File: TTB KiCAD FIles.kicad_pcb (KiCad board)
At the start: 2 copper layers, 201.2 x 86.7 mm, 10 parts, among them J1 PJ-102A, J2 Spare_Pwr_Header, J3 Mtr_Driver_Logic, J4 Relay_12V, J5 Relay_GND, J6 Mtr_Driver_Pwr

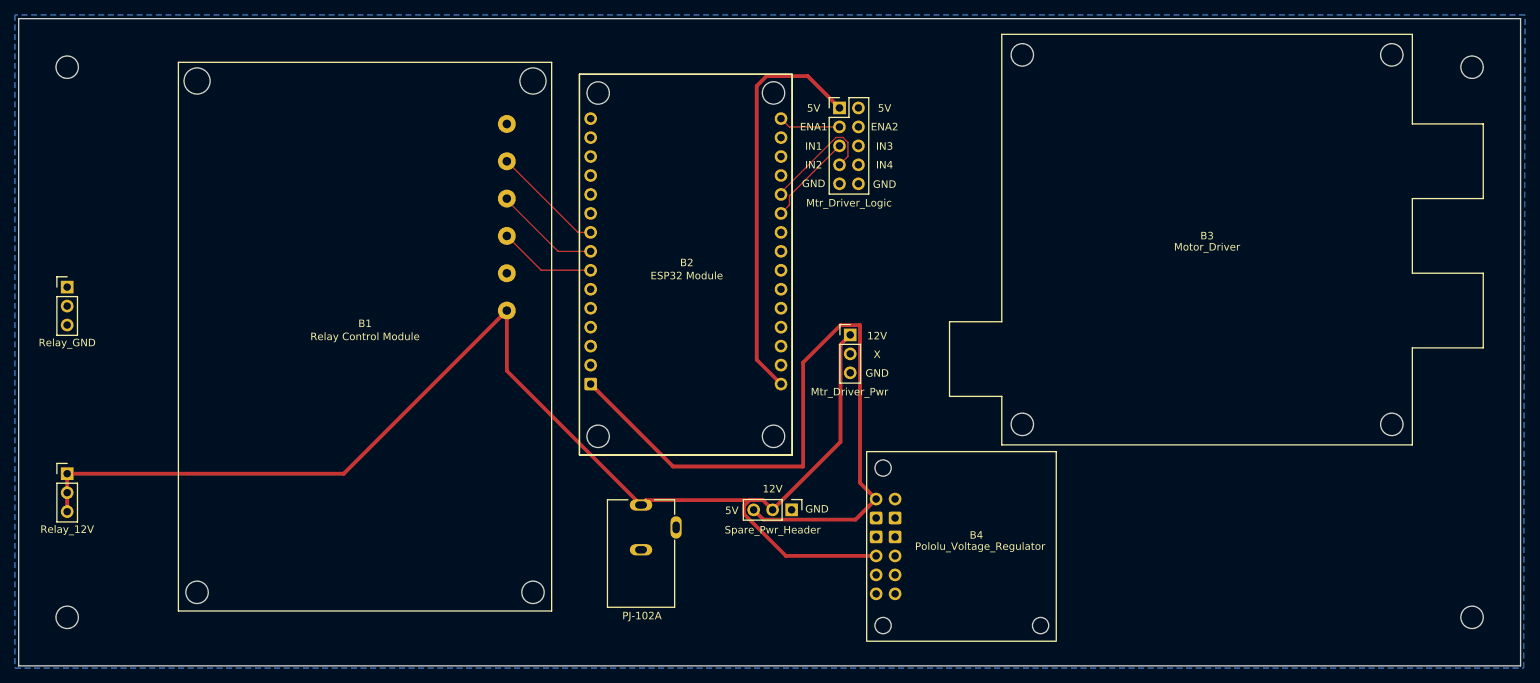
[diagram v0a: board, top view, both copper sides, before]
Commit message: Clean up draw.io files & kicad files
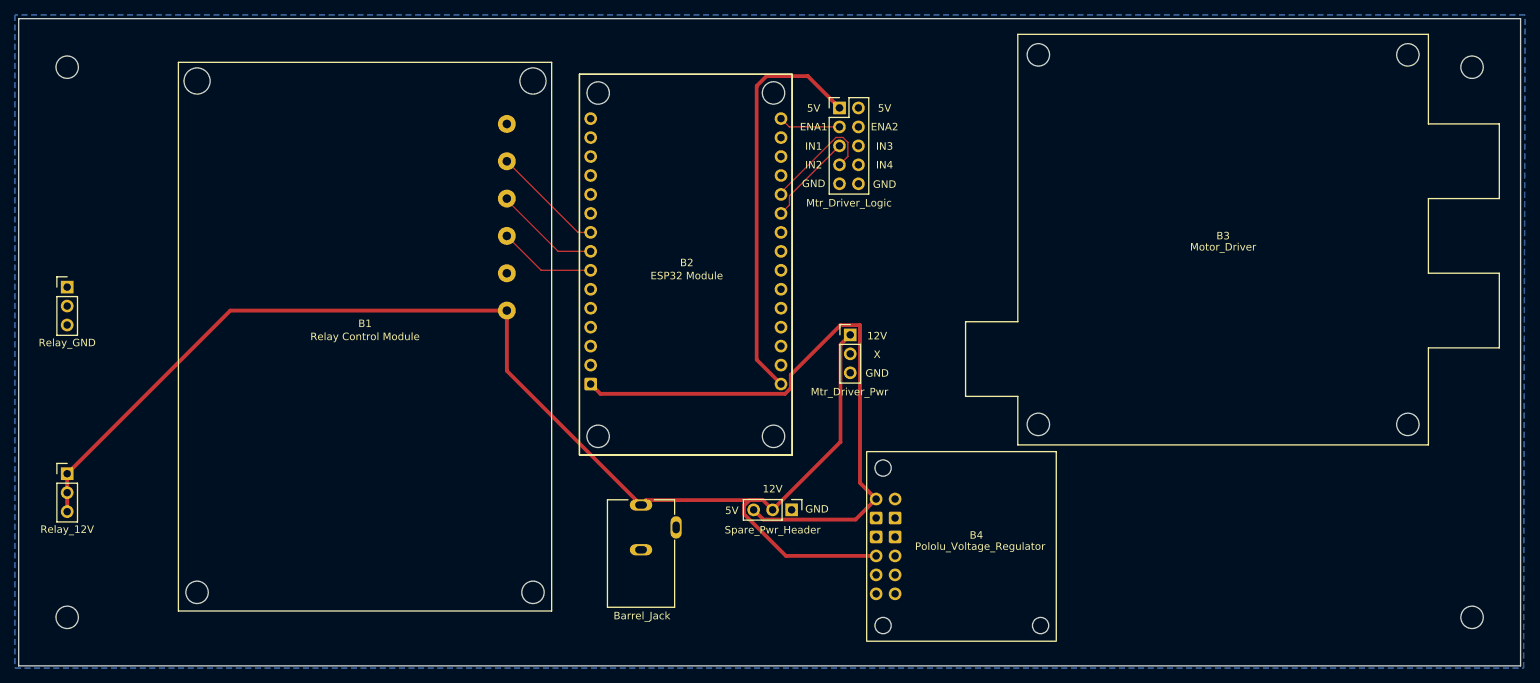
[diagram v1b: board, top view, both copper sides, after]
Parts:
- J1: value PJ-102A -> Barrel_Jack
- moved B3 2.15 mm to (201.8, 74.6)
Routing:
- net +5V: track 99.0 -> 83.8 mm
